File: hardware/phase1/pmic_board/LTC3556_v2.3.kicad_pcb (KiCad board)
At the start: 4 copper layers, 63.5 x 44.5 mm, 67 parts, among them J1 USB_B_Micro, J10 Conn_01x01_Pin, J11 Conn_01x01_Pin, J12 Conn_01x02_Pin, J13 Conn_01x03_Pin, J14 Conn_01x01_Pin, J15 Conn_01x01_Pin, J16 Conn_01x01_Pin, J17 Conn_01x01_Pin, J18 Screw_Terminal_01x02, J19 Conn_01x02_Pin, J2 Conn_01x01_Pin, J20 Screw_Terminal_01x04, J21 Screw_Terminal_01x02, J3 Conn_01x01_Pin, J4 Conn_01x01_Pin, J5 Conn_01x01_Pin, J6 Conn_01x01_Pin, J7 Conn_01x01_Pin, J8 Conn_01x01_Pin, J9 Conn_01x01_Pin, Q1 SI2333DS, SW1 SW_SPDT, U1 LTC3556EUFD_PBF, U2 TC7660B

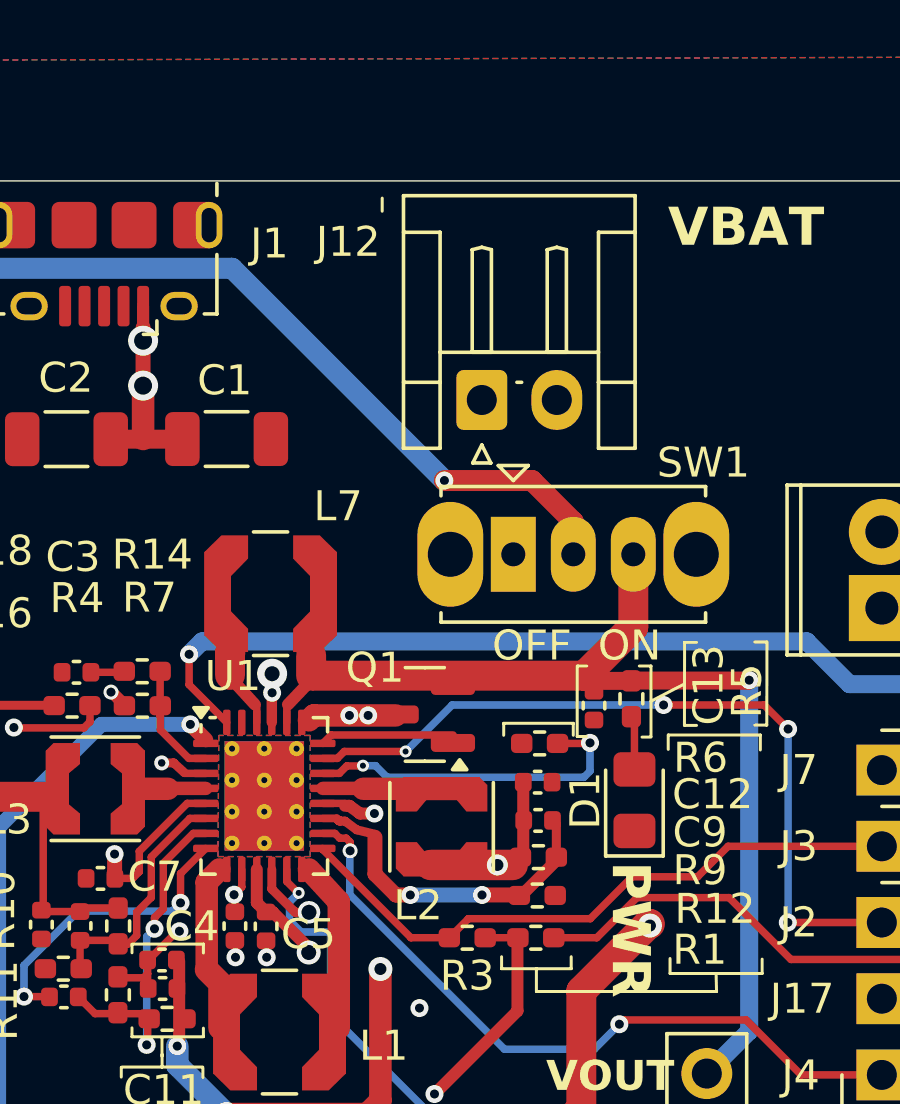
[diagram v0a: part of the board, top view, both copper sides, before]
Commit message: Update LTC to add JLC MPNs and fix JST plug
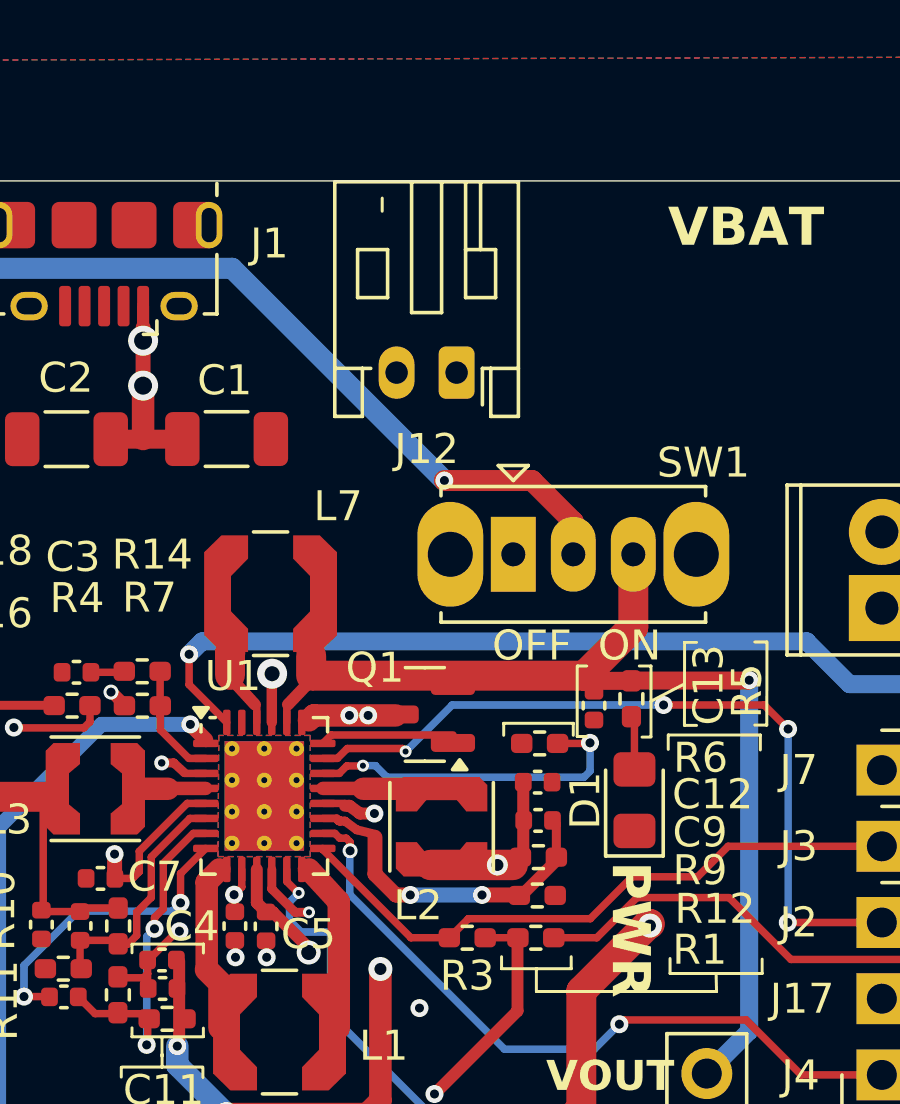
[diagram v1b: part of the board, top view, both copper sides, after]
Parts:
- J12: footprint Connector_JST:JST_EH_S2B-EH_1x02_P2.50mm_Horizontal -> Connector_JST:JST_PH_S2B-PH-K_1x02_P2.00mm_Horizontal
- TH1: value 100K -> DNP
- moved J12 1.24 mm to (147.6, 85.8), turned to 180 degrees
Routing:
- net VBAT: track 16.3 -> 15.2 mm
- net Net-(J1-VBUS): vias 5 -> 4

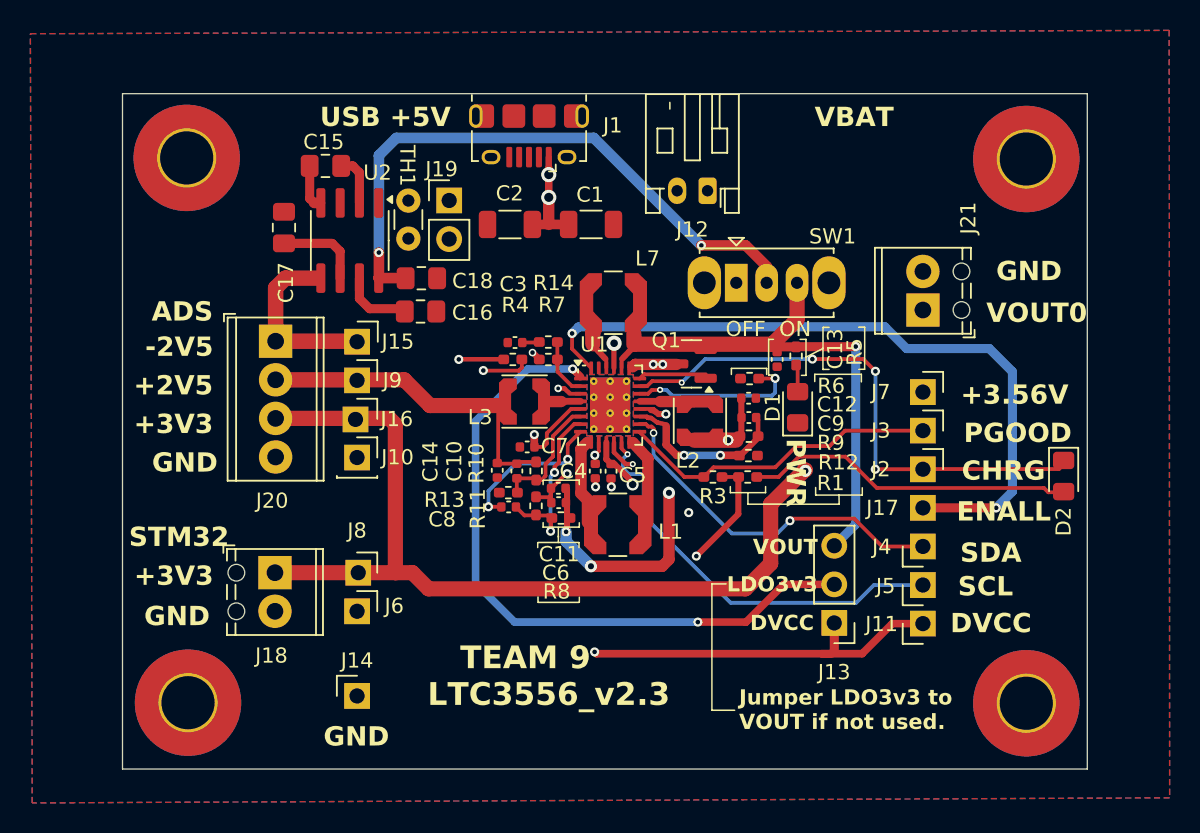
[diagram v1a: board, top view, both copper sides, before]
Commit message: Update PMIC board: edit resistor values, added MPN numbers, fixed headers
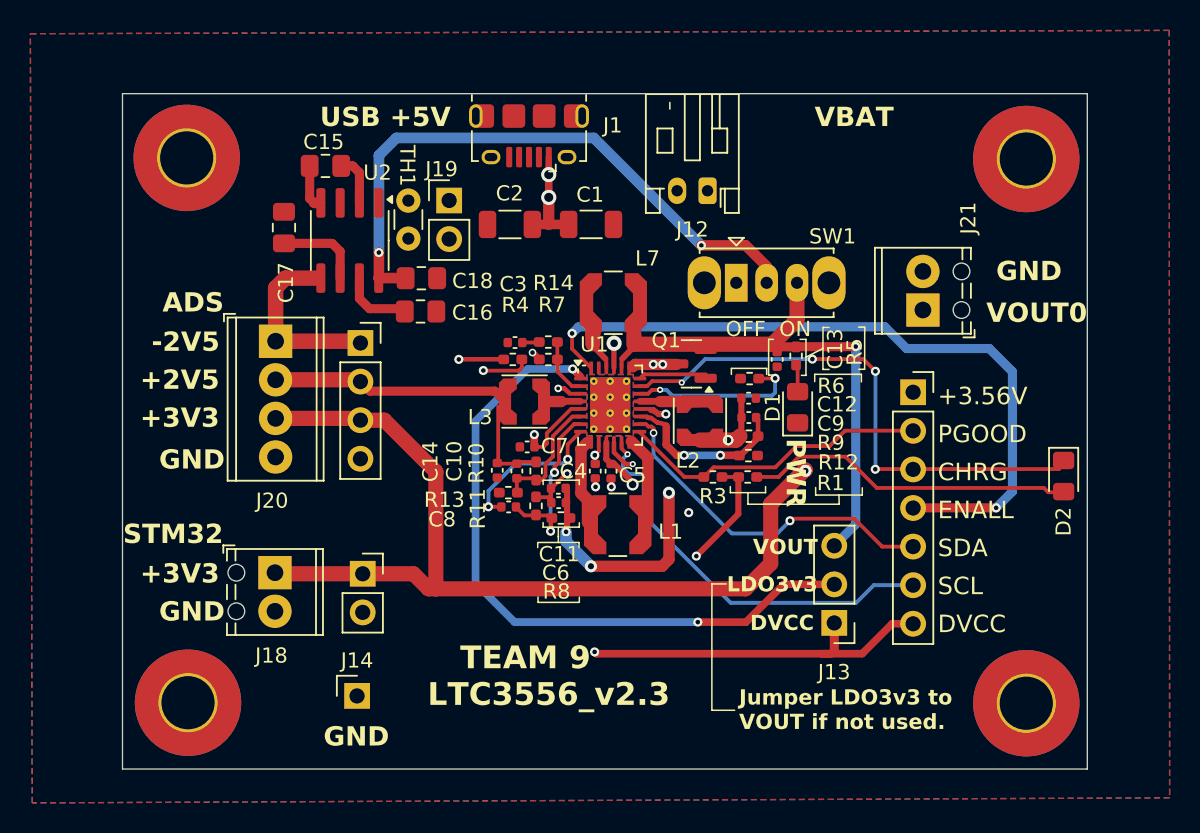
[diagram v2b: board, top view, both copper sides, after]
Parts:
- removed J10, J11, J15, J16, J17, J2, J3, J4, J5, J6, J7, J8, J9: Conn_01x01_Pin, Connector_PinSocket_2.54mm:PinSocket_1x01_P2.54mm_Vertical
- added J22: Conn_01x07, Connector_PinSocket_2.54mm:PinSocket_1x07_P2.54mm_Vertical, F.Cu at (161.1, 99.1)
- added J23: Conn_01x04, Connector_PinSocket_2.54mm:PinSocket_1x04_P2.54mm_Vertical, F.Cu at (124.8, 95.8)
- added J24: Conn_01x02, Connector_PinSocket_2.54mm:PinSocket_1x02_P2.54mm_Vertical, F.Cu at (124.9, 111.0)
- C17: value DNI -> DNP
- R10: value 235K -> 240K
- R11, R12, R13: value 111K -> 110K
- R9: value 347K -> 350K
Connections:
- net Net-(D2-K) renamed /CHRG
- net Net-(J11-Pin_1) renamed /DVCC
- net Net-(J15-Pin_1) renamed /N2V5
- net Net-(J16-Pin_1) renamed /3V3
- net Net-(J20-Pin_2) renamed /P2V5
- net Net-(J3-Pin_1) renamed /PGOOD
- net Net-(J7-Pin_1) renamed /3V56
- U1 pad 13: Net-(J5-Pin_1) -> /SCL
- U1 pad 16: Net-(J4-Pin_1) -> /SDA
- U1 pad 28: Net-(J17-Pin_1) -> /ENALL
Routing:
- net /ENALL: track 0.00 -> 48.0 mm, vias 0 -> 2
- net Net-(J17-Pin_1): track 47.4 -> 0.00 mm, vias 2 -> 0
- net Net-(J5-Pin_1): track 27.5 -> 0.00 mm, vias 1 -> 0
- net /SCL: track 0.00 -> 26.9 mm, vias 0 -> 1
- net Net-(J4-Pin_1): track 23.7 -> 0.00 mm, vias 2 -> 0
- net /SDA: track 0.00 -> 23.1 mm, vias 0 -> 2
- net Net-(J21-Pin_1): track 122.9 -> 125.2 mm
- net /3V3: track 77.0 -> 78.6 mm
- net /3V56: track 61.9 -> 61.3 mm
- net /DVCC: track 40.8 -> 40.1 mm
- net /PGOOD: track 21.1 -> 20.5 mm
